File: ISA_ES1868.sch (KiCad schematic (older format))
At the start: 107 parts, among them J1 LINE IN, J10 Volume buttons, J11 ISA BUS, J2 MIC, J3 Joystick/MIDI, J5 Wavetable, J7 SPKR OUT, J8 LINE OUT, U1 L78L05_TO92, U2 74LS138, U3 ES1868F, U4 93LC66, U7 LM1877, Y1 14.318Mhz

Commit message: Complete schematics, assigned footprints
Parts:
- removed J1: LINE IN, symbol Connector:AudioJack3
- removed J2: MIC, symbol Connector:AudioJack3
- removed J7: SPKR OUT, symbol Connector:AudioJack3
- removed J8: LINE OUT, symbol Connector:AudioJack3
- added J1: LINE IN, My_Components:Conn_Audio_3.5mm_Stereo_SJ1-352XNG, symbol my_components:JACK_TRS_3PINS
- added J2: MIC, My_Components:Conn_Audio_3.5mm_Stereo_SJ1-352XNG, symbol my_components:JACK_TRS_3PINS
- added J7: SPKR OUT, My_Components:Conn_Audio_3.5mm_Stereo_SJ1-352XNG, symbol my_components:JACK_TRS_3PINS
- added J8: LINE OUT, My_Components:Conn_Audio_3.5mm_Stereo_SJ1-352XNG, symbol my_components:JACK_TRS_3PINS
- C15, C16: footprint Capacitor_THT:C_Disc_D6.0mm_W2.5mm_P5.00mm -> Capacitor_THT:C_Disc_D3.8mm_W2.6mm_P2.50mm
- JP1, JP2: footprint (none) -> Jumper:SolderJumper-3_P1.3mm_Open_RoundedPad1.0x1.5mm_NumberLabels
- R1, R10, R11, R12, R13, R14, R15, R16, R17, R18, R2, R22, R23, R24, R25, R26, R27, R28, R29, R3, R30, R31, R32, R33, R34, R35, R36, R37, R4, R5, R6, R7, R8, R9: footprint (none) -> Resistor_THT:R_Axial_DIN0207_L6.3mm_D2.5mm_P7.62mm_Horizontal
- U3: footprint (none) -> Package_QFP:LQFP-14x20mm_P0.5mm
- U7: footprint (none) -> Package_DIP:DIP-14_W7.62mm_LongPads
- Y1: footprint (none) -> Crystal:Crystal_HC49-4H_Vertical
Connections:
- net labels added: VDDA
- wire segments 561 -> 571

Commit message: Change some output options
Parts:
- removed J8: LINE OUT, My_Components:Conn_Audio_3.5mm_Stereo_SJ1-352XNG, symbol my_components:JACK_TRS_3PINS
- added J8: LINE OUT, Connector_PinSocket_2.54mm:PinSocket_1x03_P2.54mm_Vertical, symbol Connector_Generic:Conn_01x03
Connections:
- net GNDA: now also J8.3 (Pin_3)
- net at C36.2: now also J8.1 (Pin_1)
- net at C37.2: now also J8.2 (Pin_2)
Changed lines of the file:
@@
 $EndComp
 Wire Wire Line
-	14950 8100 14950 8200
+	14950 8600 14950 8700
 $Comp
 L power:GNDA #PWR0108
 U 1 1 60AA8358
-P 14950 8200
-F 0 "#PWR0108" H 14950 7950 50  0001 C CNN
-F 1 "GNDA" H 15100 8150 50  0000 C CNN
-F 2 "" H 14950 8200 50  0001 C CNN
-F 3 "" H 14950 8200 50  0001 C CNN
-	1    14950 8200
+P 14950 8700
+F 0 "#PWR0108" H 14950 8450 50  0001 C CNN
+F 1 "GNDA" H 15100 8650 50  0000 C CNN
+F 2 "" H 14950 8700 50  0001 C CNN
+F 3 "" H 14950 8700 50  0001 C CNN
+	1    14950 8700
 	1    0    0    -1
 $EndComp
@@
 Wire Wire Line
 	21300 6300 21300 6550
-$Comp
-L my_components:JACK_TRS_3PINS J8
-U 1 1 62A78472
-P 15950 8300
-F 0 "J8" H 15572 8259 50  0000 R CNN
-F 1 "LINE OUT" H 15572 8350 50  0000 R CNN
-F 2 "My_Components:Conn_Audio_3.5mm_Stereo_SJ1-352XNG" H 15572 8396 50  0001 R CNN
-F 3 "" H 16100 8450 50  0000 C CNN
-	1    15950 8300
-	-1   0    0    1
-$EndComp
-Wire Wire Line
-	14950 8400 15300 8400
-Wire Wire Line
-	15300 8400 15300 8200
-Wire Wire Line
-	15300 8200 15500 8200
-Wire Wire Line
-	14950 8100 15500 8100
+Wire Wire Line
+	14950 8600 15500 8600
 $Comp
 L my_components:JACK_TRS_3PINS J2
@@
 Text Label 13500 4650 0    50   ~ 0
 VDDA
+$Comp
+L Connector_Generic:Conn_01x03 J8
+U 1 1 633797AC
+P 15700 8500
+F 0 "J8" H 15780 8542 50  0000 L CNN
+F 1 "LINE OUT" H 15780 8451 50  0000 L CNN
+F 2 "Connector_PinSocket_2.54mm:PinSocket_1x03_P2.54mm_Vertical" H 15700 8500 50  0001 C CNN
+F 3 "~" H 15700 8500 50  0001 C CNN
+	1    15700 8500
+	1    0    0    -1
+$EndComp
+Wire Wire Line
+	14950 8400 15500 8400
 $EndSCHEMATC

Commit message: Begin organizing PCB
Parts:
- L1: value Ferrite Bead -> Filter
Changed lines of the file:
@@
 P 7600 8550
 F 0 "L1" H 7700 8596 50  0000 L CNN
-F 1 "Ferrite Bead" H 7700 8505 50  0000 L CNN
+F 1 "Filter" H 7700 8505 50  0000 L CNN
 F 2 "Inductor_THT:L_Axial_L5.3mm_D2.2mm_P7.62mm_Horizontal_Vishay_IM-1" V 7530 8550 50  0001 C CNN
 F 3 "~" H 7600 8550 50  0001 C CNN

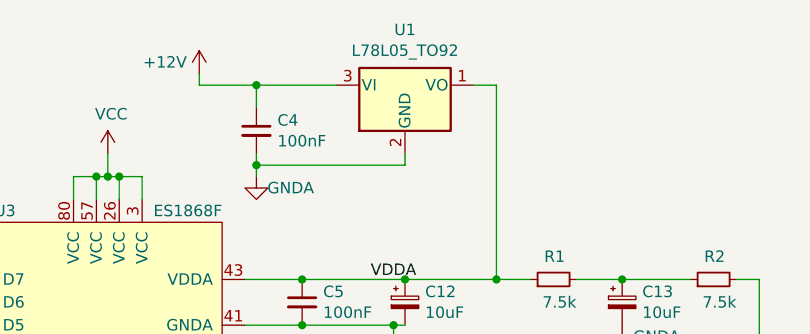
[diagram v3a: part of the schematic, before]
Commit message: More board component placement
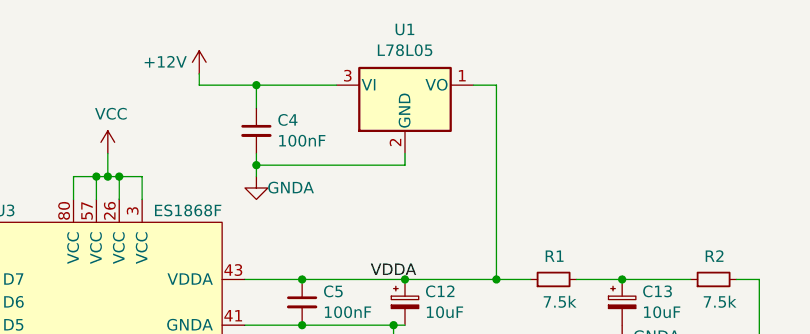
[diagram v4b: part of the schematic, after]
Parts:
- U1: value L78L05_TO92 -> L78L05
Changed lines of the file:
@@
 P 13650 3800
 F 0 "U1" H 13650 4042 50  0000 C CNN
-F 1 "L78L05_TO92" H 13650 3951 50  0000 C CNN
+F 1 "L78L05" H 13650 3951 50  0000 C CNN
 F 2 "Package_TO_SOT_THT:TO-92_Inline" H 13650 4025 50  0001 C CIN
 F 3 "http://www.st.com/content/ccc/resource/technical/document/datasheet/15/55/e5/aa/23/5b/43/fd/CD00000446.pdf/files/CD00000446.pdf/jcr:content/translations/en.CD00000446.pdf" H 13650 3750 50  0001 C CNN

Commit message: Routed audio traces
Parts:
- removed C54: 10uF, Capacitor_THT:CP_Radial_D5.0mm_P2.50mm, symbol Device:CP_Small
- removed C55: 100nF, Capacitor_THT:C_Disc_D6.0mm_W2.5mm_P5.00mm, symbol Device:C_Small
- C34, C35: footprint Capacitor_THT:CP_Radial_D5.0mm_P2.50mm -> Capacitor_THT:CP_Radial_D8.0mm_P3.50mm
- L2, L3: value Ferrite Bead -> Filter
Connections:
- net Filtered_12V: now reaches C42.1, L2.2, U7.14 (V+)
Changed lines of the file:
@@
 F 0 "C35" V 20650 7500 50  0000 L CNN
 F 1 "470uF" V 20650 7150 50  0000 L CNN
-F 2 "Capacitor_THT:CP_Radial_D5.0mm_P2.50mm" H 20600 7400 50  0001 C CNN
+F 2 "Capacitor_THT:CP_Radial_D8.0mm_P3.50mm" H 20600 7400 50  0001 C CNN
 F 3 "~" H 20600 7400 50  0001 C CNN
 	1    20600 7400
@@
 F 0 "C34" V 20650 6650 50  0000 L CNN
 F 1 "470uF" V 20650 6300 50  0000 L CNN
-F 2 "Capacitor_THT:CP_Radial_D5.0mm_P2.50mm" H 20600 6550 50  0001 C CNN
+F 2 "Capacitor_THT:CP_Radial_D8.0mm_P3.50mm" H 20600 6550 50  0001 C CNN
 F 3 "~" H 20600 6550 50  0001 C CNN
 	1    20600 6550
@@
 P 17350 4000
 F 0 "L2" V 17500 3950 50  0000 L CNN
-F 1 "Ferrite Bead" V 17250 3800 50  0000 L CNN
+F 1 "Filter" V 17250 3800 50  0000 L CNN
 F 2 "Inductor_THT:L_Axial_L5.3mm_D2.2mm_P7.62mm_Horizontal_Vishay_IM-1" V 17280 4000 50  0001 C CNN
 F 3 "~" H 17350 4000 50  0001 C CNN
@@
 	1    0    0    -1
 $EndComp
-$Comp
-L power:+12V #PWR0138
-U 1 1 61240CC5
-P 2150 9850
-F 0 "#PWR0138" H 2150 9700 50  0001 C CNN
-F 1 "+12V" H 2165 10023 50  0000 C CNN
-F 2 "" H 2150 9850 50  0001 C CNN
-F 3 "" H 2150 9850 50  0001 C CNN
-	1    2150 9850
-	1    0    0    -1
-$EndComp
-Wire Wire Line
-	2150 9850 2150 9950
-Connection ~ 2400 9950
-Wire Wire Line
-	2400 9950 2150 9950
-Connection ~ 2400 10500
-Wire Wire Line
-	2150 10500 2150 10600
-Wire Wire Line
-	2400 10500 2150 10500
-Wire Wire Line
-	2800 10350 2800 10500
-Wire Wire Line
-	2400 10500 2400 10350
-Wire Wire Line
-	2800 10500 2400 10500
-Wire Wire Line
-	2800 9950 2800 10150
-Wire Wire Line
-	2400 9950 2800 9950
-Wire Wire Line
-	2400 9950 2400 10150
-$Comp
-L power:GND #PWR0137
-U 1 1 6116B0C1
-P 2150 10600
-F 0 "#PWR0137" H 2150 10350 50  0001 C CNN
-F 1 "GND" H 2155 10427 50  0000 C CNN
-F 2 "" H 2150 10600 50  0001 C CNN
-F 3 "" H 2150 10600 50  0001 C CNN
-	1    2150 10600
-	1    0    0    -1
-$EndComp
 Connection ~ 1350 10500
 Wire Wire Line
@@
 $EndComp
 $Comp
-L Device:C_Small C55
-U 1 1 6116B0B7
-P 2800 10250
-F 0 "C55" H 2892 10296 50  0000 L CNN
-F 1 "100nF" H 2892 10205 50  0000 L CNN
-F 2 "Capacitor_THT:C_Disc_D6.0mm_W2.5mm_P5.00mm" H 2800 10250 50  0001 C CNN
-F 3 "~" H 2800 10250 50  0001 C CNN
-	1    2800 10250
-	1    0    0    -1
-$EndComp
-$Comp
-L Device:CP_Small C54
-U 1 1 6116AF87
-P 2400 10250
-F 0 "C54" H 2488 10296 50  0000 L CNN
-F 1 "10uF" H 2488 10205 50  0000 L CNN
-F 2 "Capacitor_THT:CP_Radial_D5.0mm_P2.50mm" H 2400 10250 50  0001 C CNN
-F 3 "~" H 2400 10250 50  0001 C CNN
-	1    2400 10250
-	1    0    0    -1
-$EndComp
-$Comp
 L Device:C_Small C53
 U 1 1 61086024
@@
 P 14550 9200
 F 0 "L3" V 14700 9150 50  0000 L CNN
-F 1 "Ferrite Bead" V 14400 9000 50  0000 L CNN
+F 1 "Filter" V 14400 9000 50  0000 L CNN
 F 2 "Inductor_THT:L_Axial_L5.3mm_D2.2mm_P7.62mm_Horizontal_Vishay_IM-1" V 14480 9200 50  0001 C CNN
 F 3 "~" H 14550 9200 50  0001 C CNN
@@
 Wire Wire Line
 	14950 8400 15500 8400
+Text Label 17550 4000 0    50   ~ 0
+Filtered_12V
 $EndSCHEMATC

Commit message: Routed
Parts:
- J8: footprint Connector_PinSocket_2.54mm:PinSocket_1x03_P2.54mm_Vertical -> Connector_PinHeader_2.54mm:PinHeader_1x03_P2.54mm_Horizontal
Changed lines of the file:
@@
 F 0 "J8" H 15780 8542 50  0000 L CNN
 F 1 "LINE OUT" H 15780 8451 50  0000 L CNN
-F 2 "Connector_PinSocket_2.54mm:PinSocket_1x03_P2.54mm_Vertical" H 15700 8500 50  0001 C CNN
+F 2 "Connector_PinHeader_2.54mm:PinHeader_1x03_P2.54mm_Horizontal" H 15700 8500 50  0001 C CNN
 F 3 "~" H 15700 8500 50  0001 C CNN
 	1    15700 8500

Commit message: Change silkscreen
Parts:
- J10: value Volume buttons -> Vol. Btns
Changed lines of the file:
@@
 P 11950 12450
 F 0 "J10" H 12000 12767 50  0000 C CNN
-F 1 "Volume buttons" H 12000 12676 50  0000 C CNN
+F 1 "Vol. Btns" H 12000 12676 50  0000 C CNN
 F 2 "Connector_PinHeader_2.54mm:PinHeader_2x03_P2.54mm_Vertical" H 11950 12450 50  0001 C CNN
 F 3 "~" H 11950 12450 50  0001 C CNN

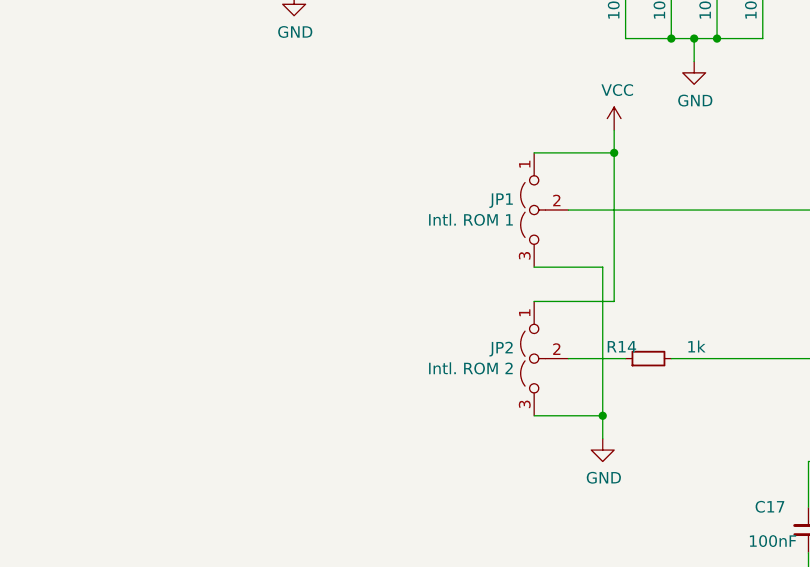
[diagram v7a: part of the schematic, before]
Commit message: More silkscreen adjustments
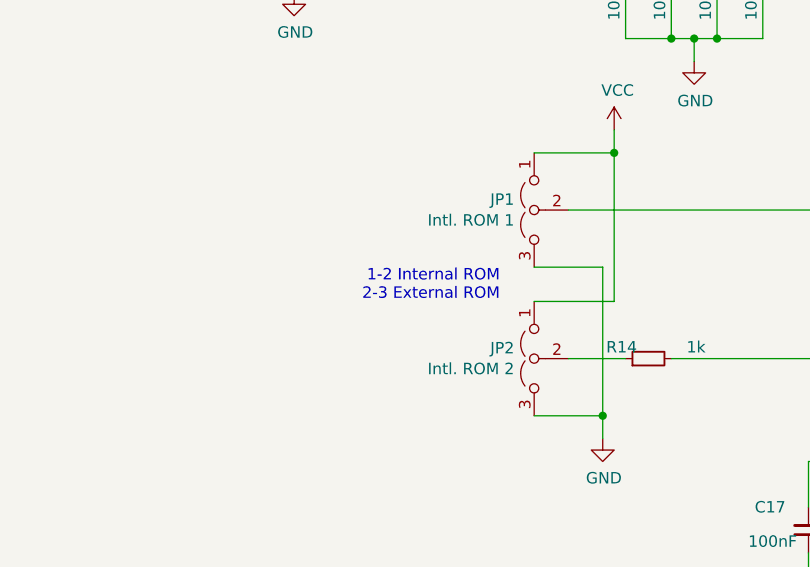
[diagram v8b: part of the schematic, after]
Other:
- note added: "1-2 Internal ROM\n2-3 External ROM"
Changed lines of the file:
@@
 Text Label 17550 4000 0    50   ~ 0
 Filtered_12V
+Text Notes 8500 11950 2    50   ~ 0
+1-2 Internal ROM\n2-3 External ROM
 $EndSCHEMATC
